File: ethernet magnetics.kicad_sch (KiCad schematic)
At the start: 18 parts, among them T1 S558-5999-46-F

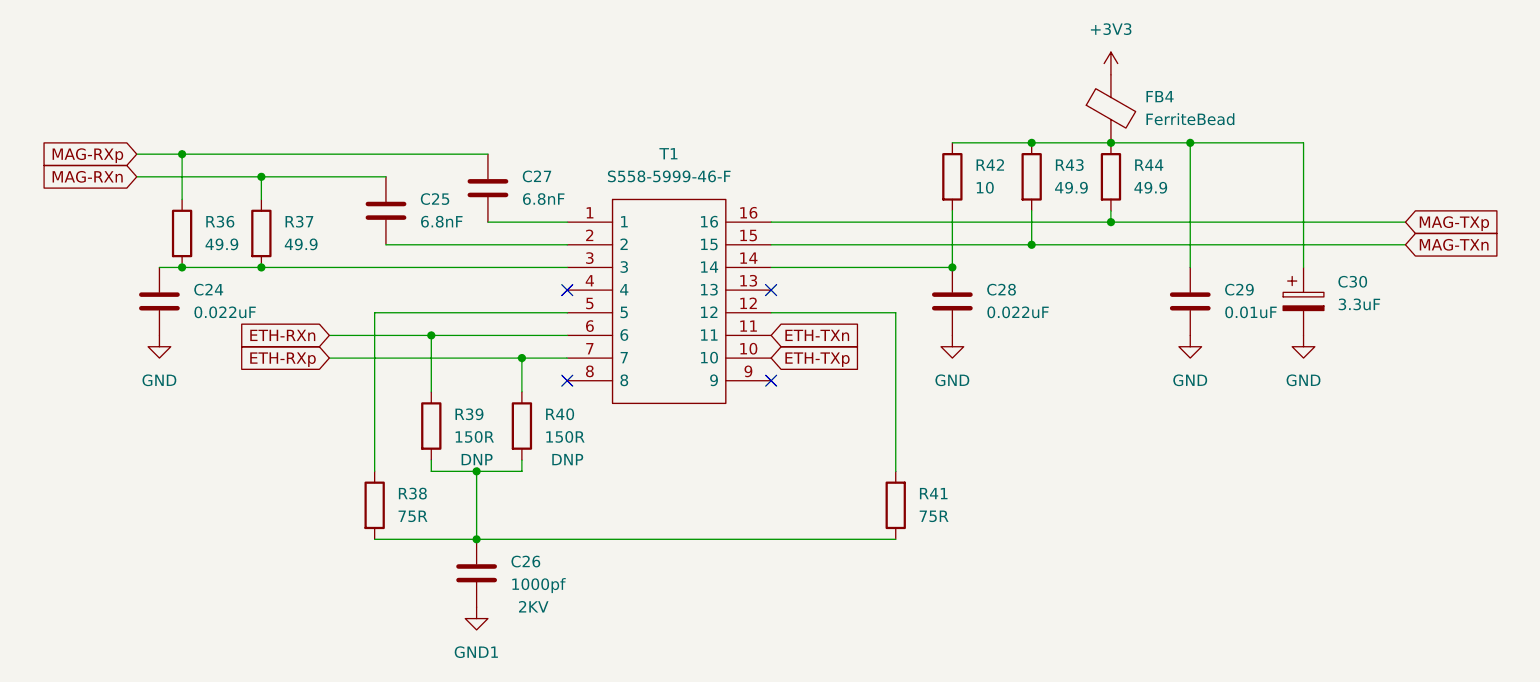
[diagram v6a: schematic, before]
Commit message: added most of the sourcing info
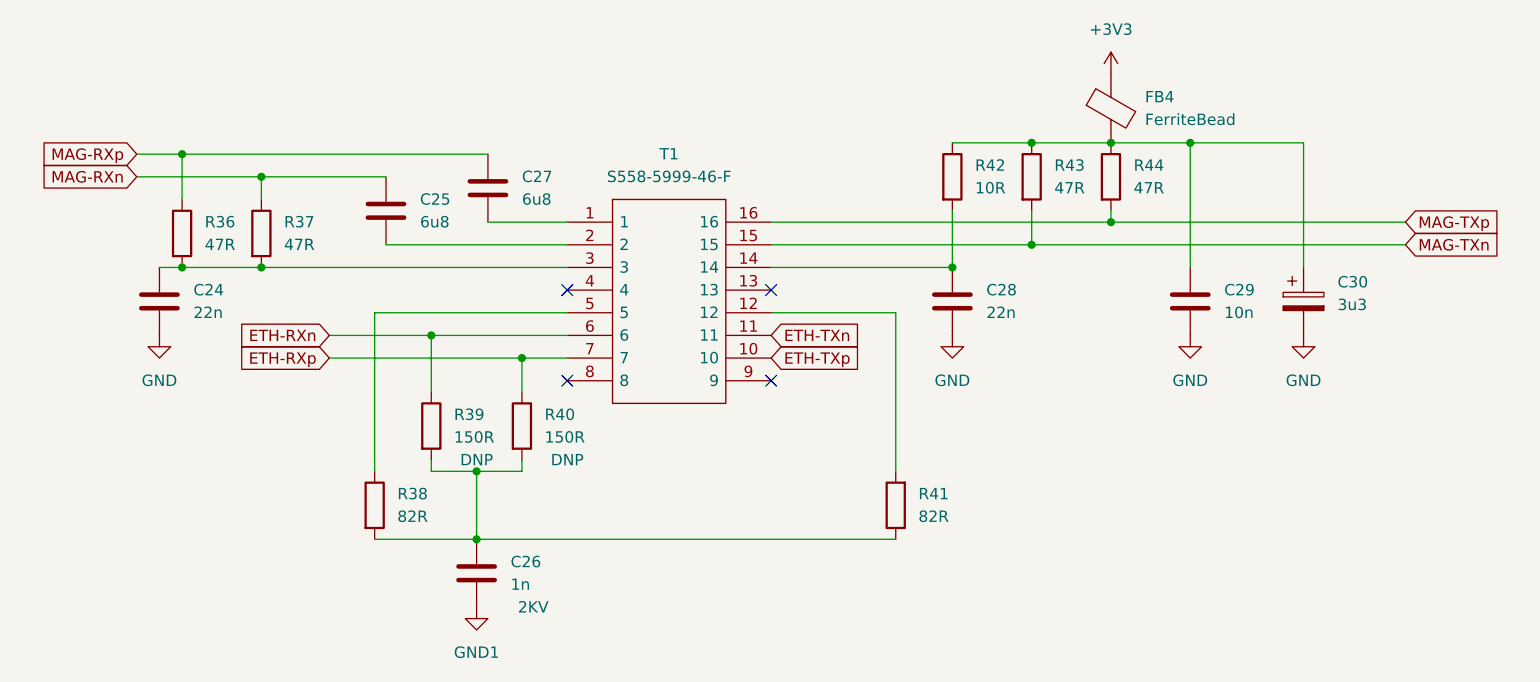
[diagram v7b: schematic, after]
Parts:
- C24, C28: value 0.022uF -> 22n; Source (none) -> L3 store
- C25, C27: value 6.8nF -> 6u8; Source (none) -> https://onecall.farnell.com/multicomp/mc0603b683k500ct/cap-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
- C26: value 1000pf -> 1n; Source (none) -> L3 store
- C29: value 0.01uF -> 10n; Source (none) -> L3 store
- C30: value 3.3uF -> 3u3; Source (none) -> L3 store
- FB4: Source (none) -> https://uk.farnell.com/bourns/mh3261-601y/ferrite-bead-0-1o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
- R36, R37, R43, R44: value 49.9 -> 47R; Source (none) -> L3 store
- R38, R41: value 75R -> 82R; Source (none) -> L3 store
- R39, R40: Source (none) -> L3 store
- R42: value 10 -> 10R; Source (none) -> L3 store
- T1: footprint Magnetics:SOP254P1270X597-16N -> SamacSys_Parts:SOP254P1270X597-16N; Source (none) -> https://uk.farnell.com/stewart-connector/s558-5999-46-f/pul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
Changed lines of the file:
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@@
       (effects (font (size 1.27 1.27)) (justify left))
     )
-    (property "Value" "6.8nF" (id 1) (at 111.76 69.8499 0)
+    (property "Value" "6u8" (id 1) (at 111.76 69.8499 0)
       (effects (font (size 1.27 1.27)) (justify left))
     )
@@
       (effects (font (size 1.27 1.27)) hide)
     )
+    (property "Source" "https://onecall.farnell.com/multicomp/mc0603b683k500ct/cap-0-068-f-50v-10-x7r-0603/dp/1759119" (id 4) (at 107.95 68.58 0)
+      (effects (font (size 1.27 1.27)) hide)
+    )
     (pin "1")
     (pin "2")
@@
       (effects (font (size 1.27 1.27)) (justify left))
     )
-    (property "Value" "75R" (id 1) (at 97.79 105.4099 0)
+    (property "Value" "82R" (id 1) (at 97.79 105.4099 0)
       (effects (font (size 1.27 1.27)) (justify left))
     )
@@
       (effects (font (size 1.27 1.27)) hide)
     )
+    (property "Source" "L3 store" (id 4) (at 95.25 104.14 0)
+      (effects (font (size 1.27 1.27)) hide)
+    )
     (pin "1")
     (pin "2")
@@
       (effects (font (size 1.27 1.27)) (justify left))
     )
-    (property "Value" "0.022uF" (id 1) (at 74.93 82.5499 0)
+    (property "Value" "22n" (id 1) (at 74.93 82.5499 0)
       (effects (font (size 1.27 1.27)) (justify left))
     )
@@
       (effects (font (size 1.27 1.27)) hide)
     )
+    (property "Source" "L3 store" (id 4) (at 71.12 81.28 0)
+      (effects (font (size 1.27 1.27)) hide)
+    )
     (pin "1")
     (pin "2")
@@
       (effects (font (size 1.27 1.27)) (justify left))
     )
-    (property "Value" "49.9" (id 1) (at 180.34 68.5799 0)
+    (property "Value" "47R" (id 1) (at 180.34 68.5799 0)
       (effects (font (size 1.27 1.27)) (justify left))
     )
@@
     )
     (property "Datasheet" "~" (id 3) (at 177.8 67.31 0)
+      (effects (font (size 1.27 1.27)) hide)
+    )
+    (property "Source" "L3 store" (id 4) (at 177.8 67.31 0)
       (effects (font (size 1.27 1.27)) hide)
     )
@@
       (effects (font (size 1.27 1.27)) (justify left))
     )
-    (property "Value" "49.9" (id 1) (at 76.2 74.9299 0)
+    (property "Value" "47R" (id 1) (at 76.2 74.9299 0)
       (effects (font (size 1.27 1.27)) (justify left))
     )
@@
     )
     (property "Datasheet" "~" (id 3) (at 73.66 73.66 0)
+      (effects (font (size 1.27 1.27)) hide)
+    )
+    (property "Source" "L3 store" (id 4) (at 73.66 73.66 0)
       (effects (font (size 1.27 1.27)) hide)
     )
@@
     (property "Reference" "T1" (id 0) (at 128.27 64.77 0))
     (property "Value" "S558-5999-46-F" (id 1) (at 128.27 67.31 0))
-    (property "Footprint" "Magnetics:SOP254P1270X597-16N" (id 2) (at 135.89 69.85 0)
+    (property "Footprint" "SamacSys_Parts:SOP254P1270X597-16N" (id 2) (at 135.89 69.85 0)
       (effects (font (size 1.27 1.27)) (justify left) hide)
     )
@@
     (property "Manufacturer_Part_Number" "S558-5999-46-F" (id 9) (at 135.89 87.63 0)
       (effects (font (size 1.27 1.27)) (justify left) hide)
+    )
+    (property "Source" "https://uk.farnell.com/stewart-connector/s558-5999-46-f/pulse-transformer-1ct-1ct-420uh/dp/2676007" (id 10) (at 116.84 72.39 0)
+      (effects (font (size 1.27 1.27)) hide)
     )
     (pin "1")
@@
       (effects (font (size 1.27 1.27)) (justify left))
     )
-    (property "Value" "0.01uF" (id 1) (at 190.5 82.5499 0)
+    (property "Value" "10n" (id 1) (at 190.5 82.5499 0)
       (effects (font (size 1.27 1.27)) (justify left))
     )
@@
     )
     (property "Datasheet" "~" (id 3) (at 186.69 81.28 0)
+      (effects (font (size 1.27 1.27)) hide)
+    )
+    (property "Source" "L3 store" (id 4) (at 186.69 81.28 0)
       (effects (font (size 1.27 1.27)) hide)
     )
@@
     )
     (property "DNP" "DNP" (id 4) (at 116.84 99.06 0))
+    (property "Source" "L3 store" (id 5) (at 111.76 95.25 0)
+      (effects (font (size 1.27 1.27)) hide)
+    )
     (pin "1")
     (pin "2")
@@
       (effects (font (size 1.27 1.27)) (justify left))
     )
-    (property "Value" "49.9" (id 1) (at 85.09 74.9299 0)
+    (property "Value" "47R" (id 1) (at 85.09 74.9299 0)
       (effects (font (size 1.27 1.27)) (justify left))
     )
@@
       (effects (font (size 1.27 1.27)) hide)
     )
+    (property "Source" "L3 store" (id 4) (at 82.55 73.66 0)
+      (effects (font (size 1.27 1.27)) hide)
+    )
     (pin "1")
     (pin "2")
@@
       (effects (font (size 1.27 1.27)) (justify left))
     )
-    (property "Value" "49.9" (id 1) (at 171.45 68.5799 0)
+    (property "Value" "47R" (id 1) (at 171.45 68.5799 0)
       (effects (font (size 1.27 1.27)) (justify left))
     )
@@
       (effects (font (size 1.27 1.27)) hide)
     )
+    (property "Source" "L3 store" (id 4) (at 168.91 67.31 0)
+      (effects (font (size 1.27 1.27)) hide)
+    )
     (pin "1")
     (pin "2")
@@
       (effects (font (size 1.27 1.27)) (justify left))
     )
-    (property "Value" "3.3uF" (id 1) (at 203.2 81.6609 0)
+    (property "Value" "3u3" (id 1) (at 203.2 81.6609 0)
       (effects (font (size 1.27 1.27)) (justify left))
     )
@@
     )
     (property "Datasheet" "~" (id 3) (at 199.39 81.28 0)
+      (effects (font (size 1.27 1.27)) hide)
+    )
+    (property "Source" "L3 store" (id 4) (at 199.39 81.28 0)
       (effects (font (size 1.27 1.27)) hide)
     )
@@
       (effects (font (size 1.27 1.27)) (justify right))
     )
-    (property "Value" "75R" (id 1) (at 156.21 105.4099 0)
+    (property "Value" "82R" (id 1) (at 156.21 105.4099 0)
       (effects (font (size 1.27 1.27)) (justify right))
     )
@@
       (effects (font (size 1.27 1.27)) hide)
     )
+    (property "Source" "L3 store" (id 4) (at 153.67 104.14 0)
+      (effects (font (size 1.27 1.27)) hide)
+    )
     (pin "1")
     (pin "2")
@@
       (effects (font (size 1.27 1.27)) (justify left))
     )
-    (property "Value" "6.8nF" (id 1) (at 100.33 72.3899 0)
+    (property "Value" "6u8" (id 1) (at 100.33 72.3899 0)
       (effects (font (size 1.27 1.27)) (justify left))
     )
@@
       (effects (font (size 1.27 1.27)) hide)
     )
+    (property "Source" "https://onecall.farnell.com/multicomp/mc0603b683k500ct/cap-0-068-f-50v-10-x7r-0603/dp/1759119" (id 4) (at 96.52 71.12 0)
+      (effects (font (size 1.27 1.27)) hide)
+    )
     (pin "1")
     (pin "2")
@@
       (effects (font (size 1.27 1.27)) (justify left))
     )
-    (property "Value" "0.022uF" (id 1) (at 163.83 82.5499 0)
+    (property "Value" "22n" (id 1) (at 163.83 82.5499 0)
       (effects (font (size 1.27 1.27)) (justify left))
     )
@@
     )
     (property "Datasheet" "~" (id 3) (at 160.02 81.28 0)
+      (effects (font (size 1.27 1.27)) hide)
+    )
+    (property "Source" "L3 store" (id 4) (at 160.02 81.28 0)
       (effects (font (size 1.27 1.27)) hide)
     )
@@
     )
     (property "DNP" "DNP" (id 4) (at 106.68 99.06 0))
+    (property "Source" "L3 store" (id 5) (at 101.6 95.25 0)
+      (effects (font (size 1.27 1.27)) hide)
+    )
     (pin "1")
     (pin "2")
@@
       (effects (font (size 1.27 1.27)) (justify left))
     )
-    (property "Value" "10" (id 1) (at 162.56 68.5799 0)
+    (property "Value" "10R" (id 1) (at 162.56 68.5799 0)
       (effects (font (size 1.27 1.27)) (justify left))
     )
@@
     )
     (property "Datasheet" "~" (id 3) (at 160.02 67.31 0)
+      (effects (font (size 1.27 1.27)) hide)
+    )
+    (property "Source" "L3 store" (id 4) (at 160.02 67.31 0)
       (effects (font (size 1.27 1.27)) hide)
     )
@@
       (effects (font (size 1.27 1.27)) (justify left))
     )
-    (property "Value" "1000pf" (id 1) (at 110.49 113.0299 0)
+    (property "Value" "1n" (id 1) (at 110.49 113.0299 0)
       (effects (font (size 1.27 1.27)) (justify left))
     )
@@
     )
     (property "Vmax" "2KV" (id 4) (at 113.03 115.57 0))
+    (property "Source" "L3 store" (id 5) (at 106.68 111.76 0)
+      (effects (font (size 1.27 1.27)) hide)
+    )
     (pin "1")
     (pin "2")
@@
       (effects (font (size 1.27 1.27)) hide)
     )
+    (property "Source" "https://uk.farnell.com/bourns/mh3261-601y/ferrite-bead-0-1ohm-2a-1206/dp/27870" (id 4) (at 177.8 59.69 0)
+      (effects (font (size 1.27 1.27)) hide)
+    )

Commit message: Create PCB
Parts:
- T1: footprint SamacSys_Parts:SOP254P1270X597-16N -> Pulse Transformer:SOP254P1270X597-16N
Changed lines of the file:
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@@
     (property "Reference" "T1" (id 0) (at 128.27 64.77 0))
     (property "Value" "S558-5999-46-F" (id 1) (at 128.27 67.31 0))
-    (property "Footprint" "SamacSys_Parts:SOP254P1270X597-16N" (id 2) (at 135.89 69.85 0)
+    (property "Footprint" "Pulse Transformer:SOP254P1270X597-16N" (id 2) (at 135.89 69.85 0)
       (effects (font (size 1.27 1.27)) (justify left) hide)
     )
